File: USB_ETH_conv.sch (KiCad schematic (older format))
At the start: 35 parts, among them CON4 RJ45-TRF-LED, U4 LAN9500A, Y2 25MHz

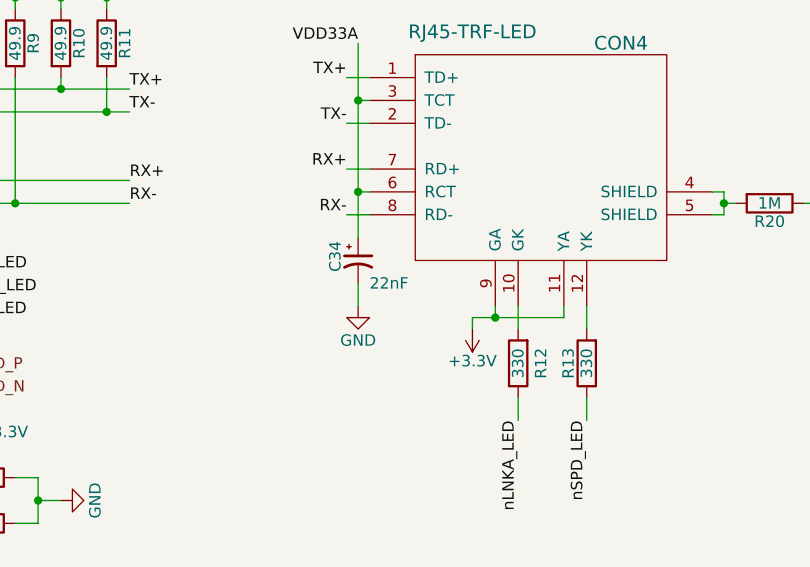
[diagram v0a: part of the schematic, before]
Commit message: Modified buck circuit on board.
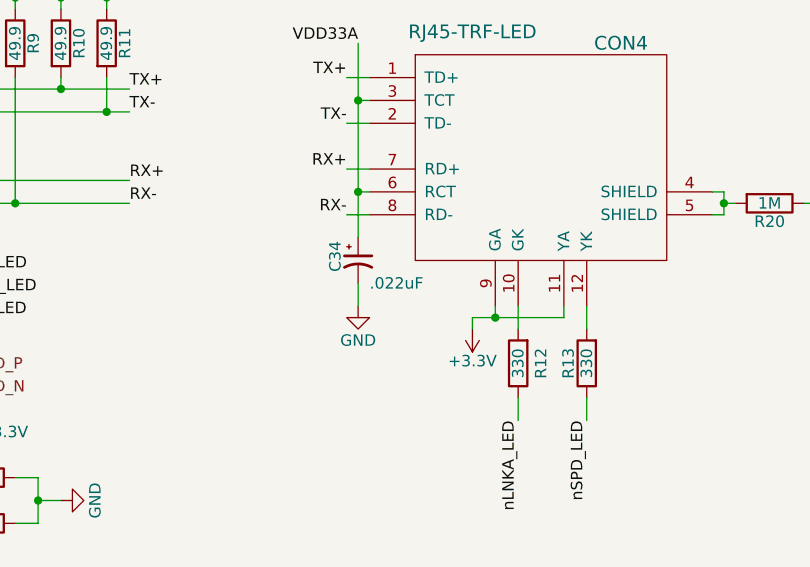
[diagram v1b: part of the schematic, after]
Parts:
- C34: value 22nF -> .022uF; footprint Capacitors_SMD:C_0805_HandSoldering -> Capacitors_SMD:C_0603_HandSoldering
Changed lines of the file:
@@
 P 6650 2650
 F 0 "C34" V 6550 2600 50  0000 L CNN
-F 1 "22nF" H 6700 2550 50  0000 L CNN
-F 2 "Capacitors_SMD:C_0805_HandSoldering" H 6650 2650 50  0001 C CNN
+F 1 ".022uF" H 6700 2550 50  0000 L CNN
+F 2 "Capacitors_SMD:C_0603_HandSoldering" H 6650 2650 50  0001 C CNN
 F 3 "" H 6650 2650 50  0000 C CNN
 	1    6650 2650

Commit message: Modified schematic. v1.1
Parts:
- added C49, C51: 100nF, Capacitors_SMD:C_0603_HandSoldering, symbol C
- C48: renamed from C34; footprint Capacitors_SMD:C_0603_HandSoldering -> Capacitors_Tantalum_SMD:CP_Tantalum_Case-C_EIA-6032-28_Hand
- renumbered C25 to C37, C26 to C38, C27 to C39, C28 to C40, C29 to C41, C30 to C42, C31 to C43, C32 to C44, C33 to C45, C35 to C46, C36 to C47, C37 to C50, C38 to C52, C39 to C53, C40 to C54, C41 to C55, D6 to D9, R6 to R26, R7 to R27, R8 to R28, R9 to R29, R10 to R30, R11 to R31, R12 to R32, R13 to R33, R20 to R34, R14 to R35, U4 to U5, W5 to W16
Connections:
- net GND: now also C49.2, C51.1
- net VDDCORE: now also C49.1
- net at CON4.4 (SHIELD), CON4.5 (SHIELD), R34.2: now also C51.2
- net TCK: no longer names the net of U5.38 (TCK/RXD1)
- net TDI: no longer names the net of U5.40 (TDI/RXD3)
- net TDO: no longer names the net of U5.37 (TDO/~nPHY_RST~)
- net TMS: no longer names the net of U5.39 (TMS/RXD2)
- net ~nTRST: no longer names the net of U5.36 (~nTRST~/RXD0)
- no-connect marks 0 -> 24
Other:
- note added: "Cate o capacitate pe fiecare pin de VDD"
- note removed: "Cate o capacitate pe fiecare bin de VDD"
- moved on the sheet: R34
